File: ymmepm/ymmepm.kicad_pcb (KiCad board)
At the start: 2 copper layers, 100 x 100 mm, 107 parts, among them J1 JTAG, J2 PMOD1, J3 PMOD2, J4 PMOD3, J5 Holes, J6 5V0G, J7 Holes, J8 Holes, J9 3V3G, SW1 KEY, SW10 KEY, SW11 KEY, SW12 KEY, SW13 KEY, SW14 KEY, SW15 KEY, SW16 KEY, SW17 KEY, SW18 KEY, SW19 KEY, SW2 KEY, SW20 KEY, SW21 KEY, SW22 KEY, SW23 KEY, SW24 KEY, SW25 KEY, SW26 KEY, SW27 KEY, SW28 KEY, SW29 KEY, SW3 KEY, SW30 KEY, SW31 KEY, SW32 KEY, SW33 KEY, SW34 KEY, SW35 KEY, SW36 KEY, SW37 KEY, SW38 KEY, SW39 KEY, SW4 KEY, SW40 KEY, SW41 KEY, SW42 KEY, SW43 KEY, SW44 KEY, SW45 KEY, SW46 KEY, SW47 KEY, SW48 KEY, SW49 KEY, SW5 KEY, SW50 KEY, SW51 KEY, SW52 KEY, SW53 KEY, SW54 KEY, SW55 KEY, SW56 KEY, SW57 KEY, SW58 KEY, SW59 KEY, SW6 KEY, SW60 KEY, SW61 KEY, SW62 KEY, SW63 KEY, SW64 KEY, SW65 KEY, SW66 KEY, SW67 KEY, SW68 KEY, SW69 KEY, SW7 KEY, SW70 KEY, SW71 KEY, SW72 KEY, SW73 KEY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

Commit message: Continue
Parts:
- removed C1, C10, C11, C12, C13, C14, C15, C2, C3, C4, C5, C6, C7, C8, C9: C, Capacitor_SMD:C_0603_1608Metric_Pad1.08x0.95mm_HandSolder
- removed C16: C0402, Capacitor_SMD:C_0402_1005Metric_Pad0.74x0.62mm_HandSolder
- removed J1: JTAG, Connector_PinSocket_2.54mm:PinSocket_2x05_P2.54mm_Vertical
- removed J2: PMOD1, Connector_PinHeader_2.54mm:PinHeader_2x06_P2.54mm_Vertical
- removed J3: PMOD2, Connector_PinHeader_2.54mm:PinHeader_2x06_P2.54mm_Vertical
- removed J4: PMOD3, Connector_PinHeader_2.54mm:PinHeader_2x06_P2.54mm_Vertical
- removed J6: 5V0G, Connector_PinHeader_2.54mm:PinHeader_1x02_P2.54mm_Vertical
- removed J9: 3V3G, Connector_PinHeader_2.54mm:PinHeader_1x02_P2.54mm_Vertical
- removed R1, R2, R3, R4: R, Resistor_SMD:R_0603_1608Metric_Pad0.98x0.95mm_HandSolder
- removed SW1, SW10, SW11, SW12, SW13, SW14, SW15, SW16, SW17, SW18, SW19, SW2, SW20, SW21, SW22, SW23, SW24, SW25, SW26, SW27, SW28, SW29, SW3, SW30, SW31, SW32, SW33, SW34, SW35, SW36, SW37, SW38, SW39, SW4, SW40, SW41, SW42, SW43, SW44, SW45, SW46, SW47, SW48, SW49, SW5, SW50, SW51, SW52, SW53, SW54, SW55, SW56, SW57, SW58, SW59, SW6, SW60, SW61, SW62, SW63, SW64, SW65, SW66, SW67, SW68, SW69, SW7, SW70, SW71, SW72, SW73, SW74, SW8, SW9: KEY, Button_Switch_SMD:SW_Push_SPST_NO_Alps_SKRK
- removed U2: EPM570T100, Package_QFP:LQFP-100_14x14mm_P0.5mm
- removed VR1: SOT-223_AMS1117-3.3, lc_lib:SOT-223
- added '1: KEY, ymm:SW_Push_SPST_NO_Alps_SKRK_BARE, F.Cu at (152.7, 132.5)
- added -1: KEY, ymm:SW_Push_SPST_NO_Alps_SKRK_BARE, F.Cu at (149.5, 119.8)
- added /1: KEY, ymm:SW_Push_SPST_NO_Alps_SKRK_BARE, F.Cu at (147.9, 138.8)
- added ;1: KEY, ymm:SW_Push_SPST_NO_Alps_SKRK_BARE, F.Cu at (146.3, 132.5)
- added =1: KEY, ymm:SW_Push_SPST_NO_Alps_SKRK_BARE, F.Cu at (155.8, 119.8)
- added A1: KEY, ymm:SW_Push_SPST_NO_Alps_SKRK_BARE, F.Cu at (89.2, 132.5)
- added AD1: KEY, ymm:SW_Push_SPST_NO_Alps_SKRK_BARE, F.Cu at (157.4, 145.2)
- added AL1: KEY, ymm:SW_Push_SPST_NO_Alps_SKRK_BARE, F.Cu at (151.1, 145.2)
- added ALT1: KEY, ymm:SW_Push_SPST_NO_Alps_SKRK_BARE, F.Cu at (95.5, 145.2)
- added AR1: KEY, ymm:SW_Push_SPST_NO_Alps_SKRK_BARE, F.Cu at (163.8, 145.2)
- added AU1: KEY, ymm:SW_Push_SPST_NO_Alps_SKRK_BARE, F.Cu at (157.4, 138.8)
- added B1: KEY, ymm:SW_Push_SPST_NO_Alps_SKRK_BARE, F.Cu at (116.1, 138.8)
- added BS1: KEY, ymm:SW_Push_SPST_NO_Alps_SKRK_BARE, F.Cu at (163.8, 119.8)
- added C17: KEY, ymm:SW_Push_SPST_NO_Alps_SKRK_BARE, F.Cu at (103.4, 138.8)
- added C18: C, Capacitor_SMD:C_0603_1608Metric_Pad1.08x0.95mm_HandSolder, F.Cu at (97.0, 88.1)
- added C19: C0402, Capacitor_SMD:C_0402_1005Metric_Pad0.74x0.62mm_HandSolder, F.Cu at (104.6, 88.1)
- added CTRL1: KEY, ymm:SW_Push_SPST_NO_Alps_SKRK_BARE, F.Cu at (79.6, 145.2)
- added D1: KEY, ymm:SW_Push_SPST_NO_Alps_SKRK_BARE, F.Cu at (101.9, 132.5)
- added D2: LED, LED_SMD:LED_0603_1608Metric_Pad1.05x0.95mm_HandSolder, F.Cu at (172.8, 105.9)
- added D3: LED, LED_SMD:LED_0603_1608Metric_Pad1.05x0.95mm_HandSolder, F.Cu at (172.8, 108.3)
- added E1: KEY, ymm:SW_Push_SPST_NO_Alps_SKRK_BARE, F.Cu at (100.3, 126.1)
- added ESC1: KEY, ymm:SW_Push_SPST_NO_Alps_SKRK_BARE, F.Cu at (79.6, 132.5)
- added ETR1: KEY, ymm:SW_Push_SPST_NO_Alps_SKRK_BARE, F.Cu at (163.8, 132.5)
- added F1: KEY, ymm:SW_Push_SPST_NO_Alps_SKRK_BARE, F.Cu at (108.2, 132.5)
- added FN1: KEY, ymm:SW_Push_SPST_NO_Alps_SKRK_BARE, F.Cu at (103.4, 145.2)
- added G1: KEY, ymm:SW_Push_SPST_NO_Alps_SKRK_BARE, F.Cu at (114.6, 132.5)
- added H1: KEY, ymm:SW_Push_SPST_NO_Alps_SKRK_BARE, F.Cu at (120.9, 132.5)
- added I1: KEY, ymm:SW_Push_SPST_NO_Alps_SKRK_BARE, F.Cu at (132.0, 126.1)
- added J11: KEY, ymm:SW_Push_SPST_NO_Alps_SKRK_BARE, F.Cu at (127.3, 132.5)
- added J12: DUMMY, ymm:PinHeader_2x10_P2.54mm_Vertical_BARE, F.Cu at (40.8, 127.8)
- added J13: JP1, Connector_PinHeader_2.54mm:PinHeader_1x02_P2.54mm_Vertical, F.Cu at (172.7, 97.5)
- added J14: JP2, Connector_PinHeader_2.54mm:PinHeader_1x02_P2.54mm_Vertical, F.Cu at (172.7, 101.3)
- added K1: KEY, ymm:SW_Push_SPST_NO_Alps_SKRK_BARE, F.Cu at (133.6, 132.5)
- added L1: KEY, ymm:SW_Push_SPST_NO_Alps_SKRK_BARE, F.Cu at (140.0, 132.5)
- added M1: KEY, ymm:SW_Push_SPST_NO_Alps_SKRK_BARE, F.Cu at (128.8, 138.8)
- added N1: KEY, ymm:SW_Push_SPST_NO_Alps_SKRK_BARE, F.Cu at (122.5, 138.8)
- added O1: KEY, ymm:SW_Push_SPST_NO_Alps_SKRK_BARE, F.Cu at (138.4, 126.1)
- added P1: KEY, ymm:SW_Push_SPST_NO_Alps_SKRK_BARE, F.Cu at (144.7, 126.1)
- added Q1: KEY, ymm:SW_Push_SPST_NO_Alps_SKRK_BARE, F.Cu at (87.6, 126.1)
- added R10: R, Resistor_SMD:R_0603_1608Metric_Pad0.98x0.95mm_HandSolder, B.Cu at (107.0, 114.3)
- added R11: R, Resistor_SMD:R_0603_1608Metric_Pad0.98x0.95mm_HandSolder, B.Cu at (81.3, 149.9)
- added R12: R, Resistor_SMD:R_0603_1608Metric_Pad0.98x0.95mm_HandSolder, B.Cu at (113.4, 114.3)
- added R13: R, Resistor_SMD:R_0603_1608Metric_Pad0.98x0.95mm_HandSolder, B.Cu at (89.8, 149.9)
- added R14: R, Resistor_SMD:R_0603_1608Metric_Pad0.98x0.95mm_HandSolder, B.Cu at (119.7, 114.3)
- added R15: R, Resistor_SMD:R_0603_1608Metric_Pad0.98x0.95mm_HandSolder, B.Cu at (98.3, 149.9)
- added R16: R, Resistor_SMD:R_0603_1608Metric_Pad0.98x0.95mm_HandSolder, B.Cu at (126.0, 114.3)
- added R17: R, Resistor_SMD:R_0603_1608Metric_Pad0.98x0.95mm_HandSolder, B.Cu at (106.8, 149.9)
- added R18: R, Resistor_SMD:R_0603_1608Metric_Pad0.98x0.95mm_HandSolder, B.Cu at (132.4, 114.3)
- added R19: R, Resistor_SMD:R_0603_1608Metric_Pad0.98x0.95mm_HandSolder, B.Cu at (115.3, 149.9)
- added R20: R, Resistor_SMD:R_0603_1608Metric_Pad0.98x0.95mm_HandSolder, B.Cu at (138.7, 114.3)
- added R21: R, Resistor_SMD:R_0603_1608Metric_Pad0.98x0.95mm_HandSolder, B.Cu at (140.8, 149.9)
- added R22: R, Resistor_SMD:R_0603_1608Metric_Pad0.98x0.95mm_HandSolder, B.Cu at (145.0, 114.3)
- added R23: R, Resistor_SMD:R_0603_1608Metric_Pad0.98x0.95mm_HandSolder, B.Cu at (149.3, 149.9)
- added R24: R, Resistor_SMD:R_0603_1608Metric_Pad0.98x0.95mm_HandSolder, B.Cu at (151.4, 114.3)
- added R25: R, Resistor_SMD:R_0603_1608Metric_Pad0.98x0.95mm_HandSolder, B.Cu at (157.8, 149.9)
- added R26: R, Resistor_SMD:R_0603_1608Metric_Pad0.98x0.95mm_HandSolder, B.Cu at (157.7, 114.3)
- added R27: R, Resistor_SMD:R_0603_1608Metric_Pad0.98x0.95mm_HandSolder, B.Cu at (166.3, 149.9)
- added R28: R, Resistor_SMD:R_0603_1608Metric_Pad0.98x0.95mm_HandSolder, B.Cu at (164.0, 114.3)
- added R29: R, Resistor_SMD:R_0603_1608Metric_Pad0.98x0.95mm_HandSolder, B.Cu at (123.8, 149.9)
- added R30: R, Resistor_SMD:R_0603_1608Metric_Pad0.98x0.95mm_HandSolder, B.Cu at (170.3, 114.3)
- added R31: R, Resistor_SMD:R_0603_1608Metric_Pad0.98x0.95mm_HandSolder, B.Cu at (132.3, 149.9)
- added R32: R, Resistor_SMD:R_0603_1608Metric_Pad0.98x0.95mm_HandSolder, B.Cu at (165.4, 97.5)
- added R33: R, Resistor_SMD:R_0603_1608Metric_Pad0.98x0.95mm_HandSolder, B.Cu at (165.4, 101.3)
- added R34: R, Resistor_SMD:R_0603_1608Metric_Pad0.98x0.95mm_HandSolder, B.Cu at (168.0, 105.9)
- added R35: R, Resistor_SMD:R_0603_1608Metric_Pad0.98x0.95mm_HandSolder, B.Cu at (168.0, 108.3)
- added R5: KEY, ymm:SW_Push_SPST_NO_Alps_SKRK_BARE, F.Cu at (106.6, 126.1)
- added R6: R, Resistor_SMD:R_0603_1608Metric_Pad0.98x0.95mm_HandSolder, B.Cu at (81.7, 114.3)
- added R7: R, Resistor_SMD:R_0603_1608Metric_Pad0.98x0.95mm_HandSolder, B.Cu at (88.1, 114.3)
- added R8: R, Resistor_SMD:R_0603_1608Metric_Pad0.98x0.95mm_HandSolder, B.Cu at (94.4, 114.3)
- added R9: R, Resistor_SMD:R_0603_1608Metric_Pad0.98x0.95mm_HandSolder, B.Cu at (100.7, 114.3)
- added S1: KEY, ymm:SW_Push_SPST_NO_Alps_SKRK_BARE, F.Cu at (95.5, 132.5)
- added SHIFT1: KEY, ymm:SW_Push_SPST_NO_Alps_SKRK_BARE, F.Cu at (79.6, 138.8)
- added SP1: KEY, ymm:SW_Push_SPST_NO_Alps_SKRK_BARE, F.Cu at (125.7, 145.2)
- added SP2: KEY, ymm:SW_Push_SPST_NO_Alps_SKRK_BARE, F.Cu at (113.0, 145.2)
- added SUPER1: KEY, ymm:SW_Push_SPST_NO_Alps_SKRK_BARE, F.Cu at (87.8, 145.2)
- added T1: KEY, ymm:SW_Push_SPST_NO_Alps_SKRK_BARE, F.Cu at (113.0, 126.1)
- added TAB1: KEY, ymm:SW_Push_SPST_NO_Alps_SKRK_BARE, F.Cu at (79.6, 126.1)
- added U3: KEY, ymm:SW_Push_SPST_NO_Alps_SKRK_BARE, F.Cu at (125.7, 126.1)
- added USR1: KEY, ymm:SW_Push_SPST_NO_Alps_SKRK_BARE, F.Cu at (170.3, 119.8)
- added USR2: KEY, ymm:SW_Push_SPST_NO_Alps_SKRK_BARE, F.Cu at (170.3, 126.1)
- added USR3: KEY, ymm:SW_Push_SPST_NO_Alps_SKRK_BARE, F.Cu at (170.3, 132.5)
- added USR4: KEY, ymm:SW_Push_SPST_NO_Alps_SKRK_BARE, F.Cu at (170.3, 138.8)
- added USR5: KEY, ymm:SW_Push_SPST_NO_Alps_SKRK_BARE, F.Cu at (170.3, 145.2)
- added USRM1: KEY, ymm:SW_Push_SPST_NO_Alps_SKRK_BARE, F.Cu at (135.2, 145.2)
- added USRM2: KEY, ymm:SW_Push_SPST_NO_Alps_SKRK_BARE, F.Cu at (143.1, 145.2)
- added V1: KEY, ymm:SW_Push_SPST_NO_Alps_SKRK_BARE, F.Cu at (109.8, 138.8)
- added W1: KEY, ymm:SW_Push_SPST_NO_Alps_SKRK_BARE, F.Cu at (93.9, 126.1)
- added X2: KEY, ymm:SW_Push_SPST_NO_Alps_SKRK_BARE, F.Cu at (97.1, 138.8)
- added X3: Just an OSC, Oscillator:Oscillator_SMD_SeikoEpson_SG8002CE-4Pin_3.2x2.5mm, F.Cu at (100.8, 88.1)
- added Y1: KEY, ymm:SW_Push_SPST_NO_Alps_SKRK_BARE, F.Cu at (119.3, 126.1)
- added Z1: KEY, ymm:SW_Push_SPST_NO_Alps_SKRK_BARE, F.Cu at (90.7, 138.8)
- added [1: KEY, ymm:SW_Push_SPST_NO_Alps_SKRK_BARE, F.Cu at (151.1, 126.1)
- added \1: KEY, ymm:SW_Push_SPST_NO_Alps_SKRK_BARE, F.Cu at (163.8, 126.1)
- added ]1: KEY, ymm:SW_Push_SPST_NO_Alps_SKRK_BARE, F.Cu at (157.4, 126.1)
- added `1: KEY, ymm:SW_Push_SPST_NO_Alps_SKRK_BARE, F.Cu at (79.6, 119.8)
- J5, J7, J8: value Holes -> DUMMY; footprint Connector_PinHeader_2.54mm:PinHeader_2x38_P2.54mm_Vertical -> ymm:PinHeader_2x10_P2.54mm_Vertical_BARE
- X1: footprint Crystal:Crystal_SMD_3225-4Pin_3.2x2.5mm_HandSoldering -> Oscillator:Oscillator_SMD_SeikoEpson_SG8002CE-4Pin_3.2x2.5mm
- moved J5 37.9 mm to (40.8, 143.1)
- moved J7 37.9 mm to (40.8, 138.0)
- moved J8 37.9 mm to (40.8, 132.9)
- moved X1 28.7 mm to (100.8, 81.0), turned to 270 degrees
- moved U1 8.86 mm to (124.7, 83.2), turned to 180 degrees
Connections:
- U1 pad 101: (no net) -> /IO101
- U1 pad 102: (no net) -> /IO102
- U1 pad 103: (no net) -> /IO103
- U1 pad 104: (no net) -> /IO104
- U1 pad 105: (no net) -> /IO105
- U1 pad 11: (no net) -> /IO11
- U1 pad 112: (no net) -> /IO112
- U1 pad 113: (no net) -> /IO113
- U1 pad 114: (no net) -> /IO114
- U1 pad 119: (no net) -> /IO119
- U1 pad 12: (no net) -> /IO12
- U1 pad 120: (no net) -> /IO120
- U1 pad 121: (no net) -> /IO121
- U1 pad 122: (no net) -> /IO122
- U1 pad 123: (no net) -> /IO123
- U1 pad 124: (no net) -> /IO124
- U1 pad 125: (no net) -> /IO125
- U1 pad 127: (no net) -> /IO127
- U1 pad 129: (no net) -> /IO129
- U1 pad 13: (no net) -> /IO13
- U1 pad 130: (no net) -> /IO130
- U1 pad 137: (no net) -> /IO137
- U1 pad 138: (no net) -> /IO138
- U1 pad 139: (no net) -> /IO139
- U1 pad 14: (no net) -> /IO14
- U1 pad 140: (no net) -> /IO140
- U1 pad 141: (no net) -> /IO141
- U1 pad 142: (no net) -> /IO142
- U1 pad 18: (no net) -> /IO18
- U1 pad 20: (no net) -> /IO20
- U1 pad 21: (no net) -> /IO21
- U1 pad 22: (no net) -> /IO22
- U1 pad 23: (no net) -> /IO23
- U1 pad 24: (no net) -> /IO24
- U1 pad 38: (no net) -> /IO38
- U1 pad 39: (no net) -> /IO39
- U1 pad 40: (no net) -> /IO40
- U1 pad 41: (no net) -> /IO41
- U1 pad 42: (no net) -> /IO42
- U1 pad 43: (no net) -> /IO43
- U1 pad 44: (no net) -> /IO44
- U1 pad 45: (no net) -> /IO45
- U1 pad 5: (no net) -> /IO5
- U1 pad 50: (no net) -> /IO50
- U1 pad 51: (no net) -> /IO51
- U1 pad 52: (no net) -> /IO52
- U1 pad 53: (no net) -> /IO53
- U1 pad 55: (no net) -> /IO55
- U1 pad 57: (no net) -> /IO57
- U1 pad 58: (no net) -> /IO58
- U1 pad 59: (no net) -> /IO59
- U1 pad 6: (no net) -> /IO6
- U1 pad 60: (no net) -> /IO60
- U1 pad 61: (no net) -> /IO61
- U1 pad 66: (no net) -> /IO66
- U1 pad 67: (no net) -> /IO67
- U1 pad 68: (no net) -> /IO68
- U1 pad 69: (no net) -> /IO69
- U1 pad 7: (no net) -> /IO7
- U1 pad 71: (no net) -> /IO71
- U1 pad 72: (no net) -> /IO72
- U1 pad 73: (no net) -> /IO73
- U1 pad 74: (no net) -> /IO74
- U1 pad 75: (no net) -> /IO75
- U1 pad 76: (no net) -> /IO76
- U1 pad 77: (no net) -> /IO77
- U1 pad 8: (no net) -> /IO8
- U1 pad 81: (no net) -> /IO81
- U1 pad 88: (no net) -> /IO88
- U1 pad 89: (no net) -> /IO89
- U1 pad 91: (no net) -> /IO91
- U1 pad 93: (no net) -> /IO93
- U1 pad 94: (no net) -> /IO94
- U1 pad 95: (no net) -> /IO95
- U1 pad 96: (no net) -> /IO96
- U1 pad 97: (no net) -> /IO97
- U1 pad 98: (no net) -> /IO98
- X1 pad 3: (no net) -> /IO89
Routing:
- net +3V3: track 0.00 -> 554.0 mm, vias 0 -> 19
- net GND: track 0.00 -> 411.0 mm, vias 0 -> 19
- net /IO124: track 0.00 -> 204.3 mm, vias 0 -> 11
- net /IO137: track 0.00 -> 199.0 mm, vias 0 -> 3
- net /IO74: track 0.00 -> 190.9 mm, vias 0 -> 12
- net /IO138: track 0.00 -> 189.3 mm, vias 0 -> 3
- net /IO73: track 0.00 -> 181.3 mm, vias 0 -> 3
- net /IO139: track 0.00 -> 180.3 mm, vias 0 -> 3
- net /IO75: track 0.00 -> 179.7 mm, vias 0 -> 14
- net /IO76: track 0.00 -> 171.8 mm, vias 0 -> 15
- net /IO140: track 0.00 -> 166.8 mm, vias 0 -> 3
- net /IO141: track 0.00 -> 155.9 mm, vias 0 -> 3
- net /IO77: track 0.00 -> 154.5 mm, vias 0 -> 14
- net /IO142: track 0.00 -> 149.9 mm, vias 0 -> 3
- net /IO5: track 0.00 -> 145.0 mm, vias 0 -> 3
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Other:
- net class Default: clearance 0.2 -> 0.1524; trace_width 0.25 -> 0.1524; via_dia 0.8 -> 0.5588; via_drill 0.4 -> 0.3556
- net class PWR added: clearance 0.1524, trace_width 0.254, via_dia 0.5588, via_drill 0.3556
- rule trace_clearance: 0.2 -> 0.1524
- rule trace_min: 0.2 -> 0.1524
- rule via_min_drill: 0.3 -> 0.3556
- rule via_min_size: 0.4 -> 0.5588

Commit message: Near close I think
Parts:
- added J15: PMOD1, Connector_PinHeader_2.54mm:PinHeader_2x06_P2.54mm_Vertical, F.Cu at (80.0, 92.7)
- added J16: HOLE, ymm:PinHeader_1x01_P2.54mm_Vertical_BARE, F.Cu at (129.7, 65.8)
- added J17: HOLE, ymm:PinHeader_1x01_P2.54mm_Vertical_BARE, F.Cu at (127.1, 65.8)
- added J18: HOLE, ymm:PinHeader_1x01_P2.54mm_Vertical_BARE, F.Cu at (139.1, 68.5)
- added J19: HOLE, ymm:PinHeader_1x01_P2.54mm_Vertical_BARE, F.Cu at (141.6, 68.5)
- added J20: HOLE, ymm:PinHeader_1x01_P2.54mm_Vertical_BARE, F.Cu at (144.1, 68.5)
- added J21: HOLE, ymm:PinHeader_1x01_P2.54mm_Vertical_BARE, F.Cu at (144.7, 83.3)
- added J22: HOLE, ymm:PinHeader_1x01_P2.54mm_Vertical_BARE, F.Cu at (142.1, 83.3)
- added J23: HOLE, ymm:PinHeader_1x01_P2.54mm_Vertical_BARE, F.Cu at (140.0, 89.8)
- added J24: HOLE, ymm:PinHeader_1x01_P2.54mm_Vertical_BARE, F.Cu at (144.1, 65.9)
- added J25: HOLE, ymm:PinHeader_1x01_P2.54mm_Vertical_BARE, F.Cu at (146.7, 65.9)
- added J26: HOLE, ymm:PinHeader_1x01_P2.54mm_Vertical_BARE, F.Cu at (150.2, 76.1)
- added J27: HOLE, ymm:PinHeader_1x01_P2.54mm_Vertical_BARE, F.Cu at (150.2, 78.6)
- added J28: HOLE, ymm:PinHeader_1x01_P2.54mm_Vertical_BARE, F.Cu at (142.6, 89.8)
- added J29: HOLE, ymm:PinHeader_1x01_P2.54mm_Vertical_BARE, F.Cu at (145.1, 89.8)
- added J30: HOLE, ymm:PinHeader_1x01_P2.54mm_Vertical_BARE, F.Cu at (147.6, 89.8)
- added J31: HOLE, ymm:PinHeader_1x01_P2.54mm_Vertical_BARE, F.Cu at (147.6, 92.3)
- added J32: HOLE, ymm:PinHeader_1x01_P2.54mm_Vertical_BARE, F.Cu at (145.1, 92.3)
- added J33: HOLE, ymm:PinHeader_1x01_P2.54mm_Vertical_BARE, F.Cu at (99.8, 97.2)
- added J34: HOLE, ymm:PinHeader_1x01_P2.54mm_Vertical_BARE, F.Cu at (102.4, 97.2)
- added J35: HOLE, ymm:PinHeader_1x01_P2.54mm_Vertical_BARE, F.Cu at (104.9, 97.2)
- added J36: HOLE, ymm:PinHeader_1x01_P2.54mm_Vertical_BARE, F.Cu at (107.4, 97.2)
- added J37: HOLE, ymm:PinHeader_1x01_P2.54mm_Vertical_BARE, F.Cu at (100.4, 69.5)
- added J38: HOLE, ymm:PinHeader_1x01_P2.54mm_Vertical_BARE, F.Cu at (100.4, 72.0)
- added J39: HOLE, ymm:PinHeader_1x01_P2.54mm_Vertical_BARE, F.Cu at (105.5, 72.0)
- added J40: HOLE, ymm:PinHeader_1x01_P2.54mm_Vertical_BARE, F.Cu at (102.9, 72.0)
- moved J12 6.43 mm to (38.5, 121.8)
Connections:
- J12 pad 1: (no net) -> Net-(J12-Pad1)
- J12 pad 10: (no net) -> Net-(J12-Pad10)
- J12 pad 11: (no net) -> Net-(J12-Pad11)
- J12 pad 12: (no net) -> Net-(J12-Pad12)
- J12 pad 13: (no net) -> Net-(J12-Pad13)
- J12 pad 14: (no net) -> Net-(J12-Pad14)
- J12 pad 15: (no net) -> Net-(J12-Pad15)
- J12 pad 16: (no net) -> Net-(J12-Pad16)
- J12 pad 17: (no net) -> Net-(J12-Pad17)
- J12 pad 18: (no net) -> Net-(J12-Pad18)
- J12 pad 19: (no net) -> Net-(J12-Pad19)
- J12 pad 2: (no net) -> Net-(J12-Pad2)
- J12 pad 20: (no net) -> Net-(J12-Pad20)
- J12 pad 3: (no net) -> Net-(J12-Pad3)
- J12 pad 4: (no net) -> Net-(J12-Pad4)
- J12 pad 5: (no net) -> Net-(J12-Pad5)
- J12 pad 6: (no net) -> Net-(J12-Pad6)
- J12 pad 7: (no net) -> Net-(J12-Pad7)
- J12 pad 8: (no net) -> Net-(J12-Pad8)
- J12 pad 9: (no net) -> Net-(J12-Pad9)
- J5 pad 1: (no net) -> Net-(J5-Pad1)
- J5 pad 10: (no net) -> Net-(J5-Pad10)
- J5 pad 11: (no net) -> Net-(J5-Pad11)
- J5 pad 12: (no net) -> Net-(J5-Pad12)
- J5 pad 13: (no net) -> Net-(J5-Pad13)
- J5 pad 14: (no net) -> Net-(J5-Pad14)
- J5 pad 15: (no net) -> Net-(J5-Pad15)
- J5 pad 16: (no net) -> Net-(J5-Pad16)
- J5 pad 17: (no net) -> Net-(J5-Pad17)
- J5 pad 18: (no net) -> Net-(J5-Pad18)
- J5 pad 19: (no net) -> Net-(J5-Pad19)
- J5 pad 2: (no net) -> Net-(J5-Pad2)
- J5 pad 20: (no net) -> Net-(J5-Pad20)
- J5 pad 3: (no net) -> Net-(J5-Pad3)
- J5 pad 4: (no net) -> Net-(J5-Pad4)
- J5 pad 5: (no net) -> Net-(J5-Pad5)
- J5 pad 6: (no net) -> Net-(J5-Pad6)
- J5 pad 7: (no net) -> Net-(J5-Pad7)
- J5 pad 8: (no net) -> Net-(J5-Pad8)
- J5 pad 9: (no net) -> Net-(J5-Pad9)
- J7 pad 1: (no net) -> Net-(J7-Pad1)
- J7 pad 10: (no net) -> Net-(J7-Pad10)
- J7 pad 11: (no net) -> Net-(J7-Pad11)
- J7 pad 12: (no net) -> Net-(J7-Pad12)
- J7 pad 13: (no net) -> Net-(J7-Pad13)
- J7 pad 14: (no net) -> Net-(J7-Pad14)
- J7 pad 15: (no net) -> Net-(J7-Pad15)
- J7 pad 16: (no net) -> Net-(J7-Pad16)
- J7 pad 17: (no net) -> Net-(J7-Pad17)
- J7 pad 18: (no net) -> Net-(J7-Pad18)
- J7 pad 19: (no net) -> Net-(J7-Pad19)
- J7 pad 2: (no net) -> Net-(J7-Pad2)
- J7 pad 20: (no net) -> Net-(J7-Pad20)
- J7 pad 3: (no net) -> Net-(J7-Pad3)
- J7 pad 4: (no net) -> Net-(J7-Pad4)
- J7 pad 5: (no net) -> Net-(J7-Pad5)
- J7 pad 6: (no net) -> Net-(J7-Pad6)
- J7 pad 7: (no net) -> Net-(J7-Pad7)
- J7 pad 8: (no net) -> Net-(J7-Pad8)
- J7 pad 9: (no net) -> Net-(J7-Pad9)
- J8 pad 1: (no net) -> Net-(J8-Pad1)
- J8 pad 10: (no net) -> Net-(J8-Pad10)
- J8 pad 11: (no net) -> Net-(J8-Pad11)
- J8 pad 12: (no net) -> Net-(J8-Pad12)
- J8 pad 13: (no net) -> Net-(J8-Pad13)
- J8 pad 14: (no net) -> Net-(J8-Pad14)
- J8 pad 15: (no net) -> Net-(J8-Pad15)
- J8 pad 16: (no net) -> Net-(J8-Pad16)
- J8 pad 17: (no net) -> Net-(J8-Pad17)
- J8 pad 18: (no net) -> Net-(J8-Pad18)
- J8 pad 19: (no net) -> Net-(J8-Pad19)
- J8 pad 2: (no net) -> Net-(J8-Pad2)
- J8 pad 20: (no net) -> Net-(J8-Pad20)
- J8 pad 3: (no net) -> Net-(J8-Pad3)
- J8 pad 4: (no net) -> Net-(J8-Pad4)
- J8 pad 5: (no net) -> Net-(J8-Pad5)
- J8 pad 6: (no net) -> Net-(J8-Pad6)
- J8 pad 7: (no net) -> Net-(J8-Pad7)
- J8 pad 8: (no net) -> Net-(J8-Pad8)
- J8 pad 9: (no net) -> Net-(J8-Pad9)
- U1 pad 1: (no net) -> /IO1
- U1 pad 106: (no net) -> /IO106
- U1 pad 107: (no net) -> /IO107
- U1 pad 108: (no net) -> /IO108
- U1 pad 109: (no net) -> /IO109
- U1 pad 110: (no net) -> /IO110
- U1 pad 111: (no net) -> /IO111
- U1 pad 117: (no net) -> /IO117
- U1 pad 118: (no net) -> /IO118
- U1 pad 131: (no net) -> /IO131
- U1 pad 132: (no net) -> /IO132
- U1 pad 133: (no net) -> /IO133
- U1 pad 134: (no net) -> /IO134
- U1 pad 143: (no net) -> /IO143
- U1 pad 144: (no net) -> /IO144
- U1 pad 15: (no net) -> /IO15
- U1 pad 16: (no net) -> /IO16
- U1 pad 2: (no net) -> /IO2
- U1 pad 27: (no net) -> /IO27
- U1 pad 28: (no net) -> /IO28
- U1 pad 29: (no net) -> /IO29
- U1 pad 3: (no net) -> /IO3
- U1 pad 30: (no net) -> /IO30
- U1 pad 31: (no net) -> /IO31
- U1 pad 32: (no net) -> /IO32
- U1 pad 37: (no net) -> /IO37
- U1 pad 4: (no net) -> /IO4
- U1 pad 48: (no net) -> /IO48
- U1 pad 49: (no net) -> /IO49
- U1 pad 62: (no net) -> /IO62
- U1 pad 63: (no net) -> /IO63
- U1 pad 70: (no net) -> /IO70
- U1 pad 78: (no net) -> /IO78
- U1 pad 79: (no net) -> /IO79
- U1 pad 80: (no net) -> /IO80
- U1 pad 84: (no net) -> /IO84
- U1 pad 85: (no net) -> /IO85
- U1 pad 86: (no net) -> /IO86
- U1 pad 87: (no net) -> /IO87
- X1 pad 1: (no net) -> Net-(X1-Pad1)
- X3 pad 1: (no net) -> Net-(X3-Pad1)
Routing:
- net +3V3: track 554.0 -> 0.00 mm, vias 19 -> 0
- net GND: track 411.0 -> 0.00 mm, vias 19 -> 0
- net /IO124: track 204.3 -> 0.00 mm, vias 11 -> 0
- net /IO137: track 199.0 -> 0.00 mm, vias 3 -> 0
- net /IO74: track 190.9 -> 0.00 mm, vias 12 -> 0
- net /IO138: track 189.3 -> 0.00 mm, vias 3 -> 0
- net /IO73: track 181.3 -> 0.00 mm, vias 3 -> 0
- net /IO139: track 180.3 -> 0.00 mm, vias 3 -> 0
- net /IO75: track 179.7 -> 0.00 mm, vias 14 -> 0
- net /IO76: track 171.8 -> 0.00 mm, vias 15 -> 0
- net /IO140: track 166.8 -> 0.00 mm, vias 3 -> 0
- net /IO141: track 155.9 -> 0.00 mm, vias 3 -> 0
- net /IO77: track 154.5 -> 0.00 mm, vias 14 -> 0
- net /IO142: track 149.9 -> 0.00 mm, vias 3 -> 0
- net /IO5: track 145.0 -> 0.00 mm, vias 3 -> 0
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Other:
- board outline removed
- board text removed: "%regymm"

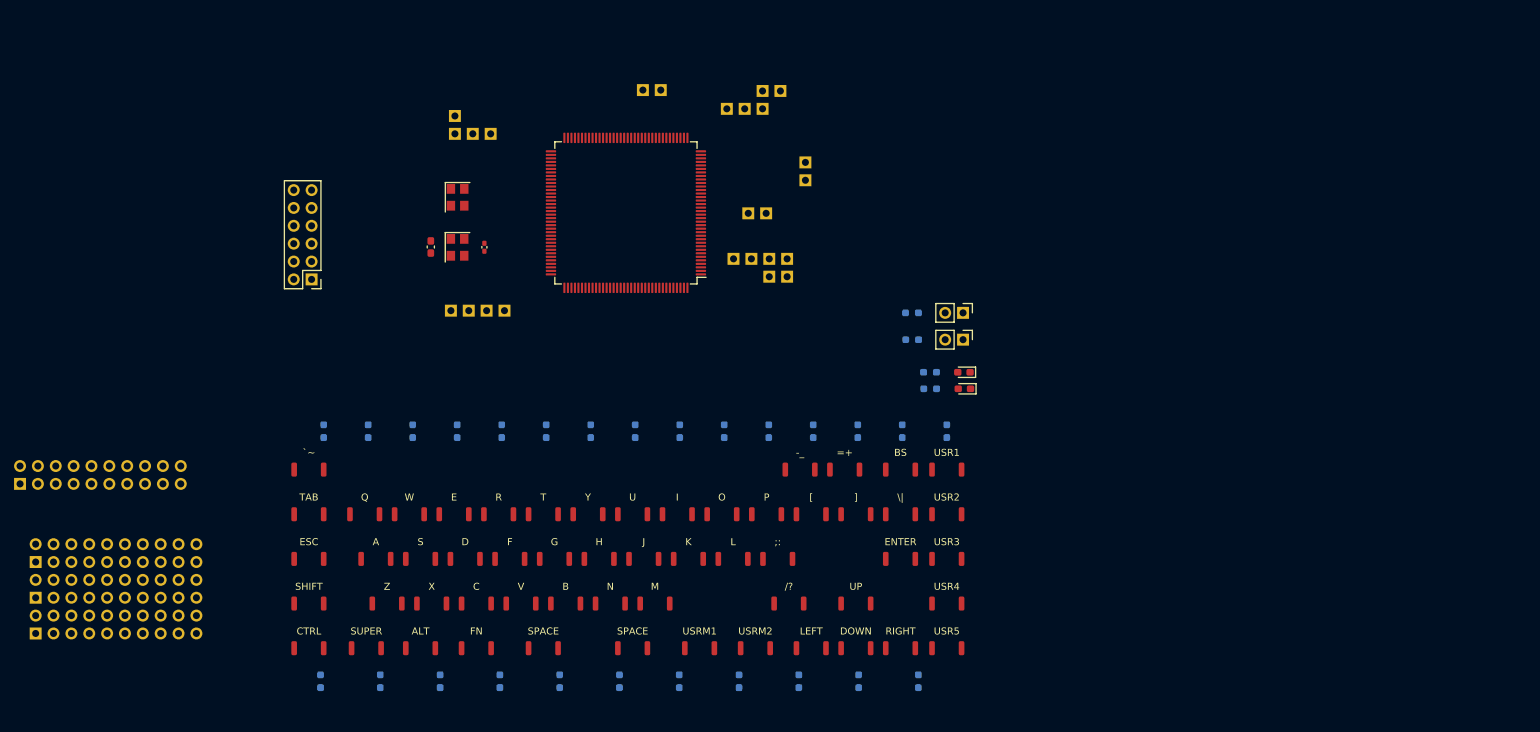
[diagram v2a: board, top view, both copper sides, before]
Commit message: Go production at JLC purple
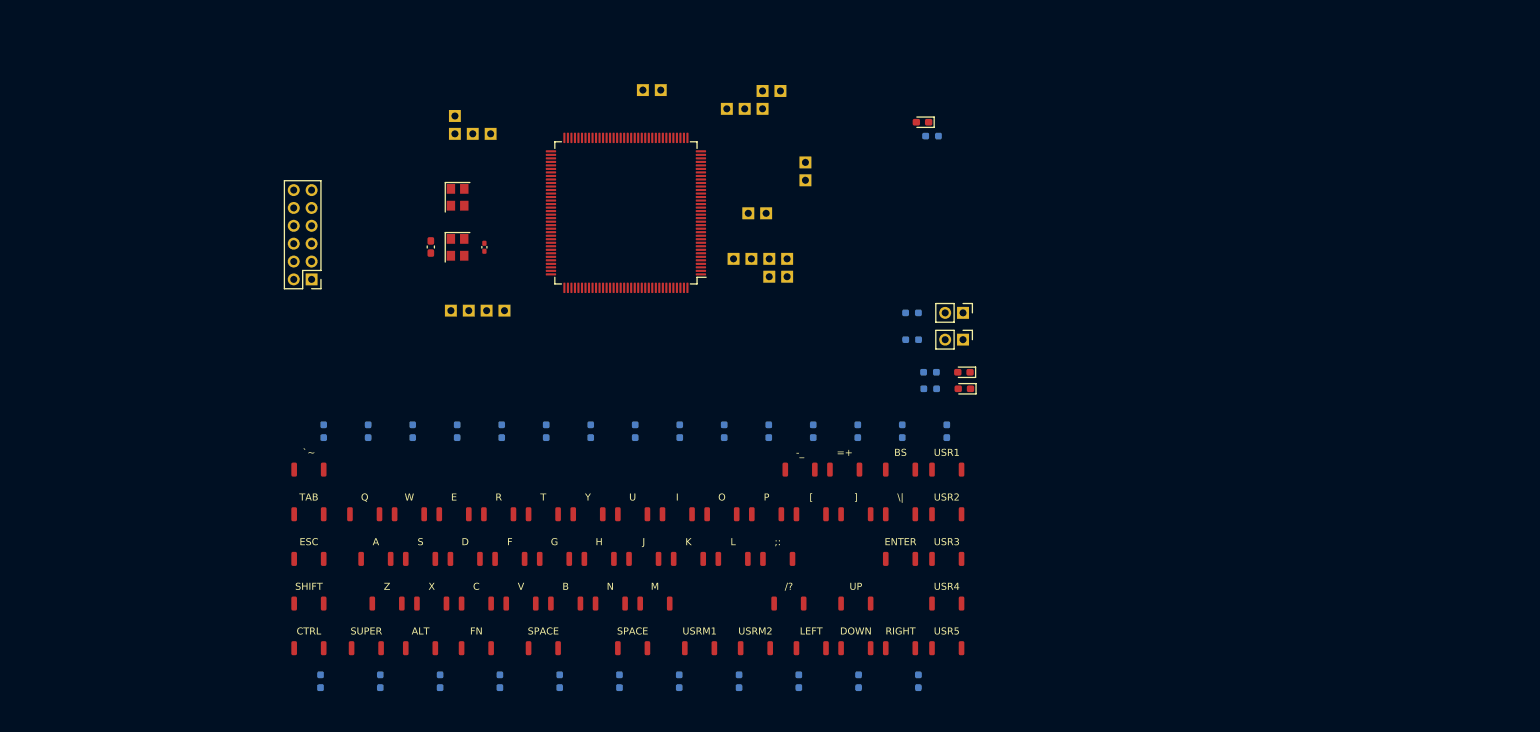
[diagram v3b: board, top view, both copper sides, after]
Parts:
- removed J12, J5, J7, J8: DUMMY, ymm:PinHeader_2x10_P2.54mm_Vertical_BARE
- added D4: LED, LED_SMD:LED_0603_1608Metric_Pad1.05x0.95mm_HandSolder, F.Cu at (166.9, 70.4)
- added R36: R, Resistor_SMD:R_0603_1608Metric_Pad0.98x0.95mm_HandSolder, B.Cu at (168.3, 72.3)
